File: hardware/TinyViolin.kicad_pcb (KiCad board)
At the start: 2 copper layers, 100 x 80 mm, 44 parts, among them J1 ICSP, J2 503182-1852, SW1 SW_SPDT, SW2 Tactile, SW3 SW_Push, SW4 SW_Push, SW5 SW_Push, SW6 SW_Push, U1 ATmega328-PU, U2 BOOST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

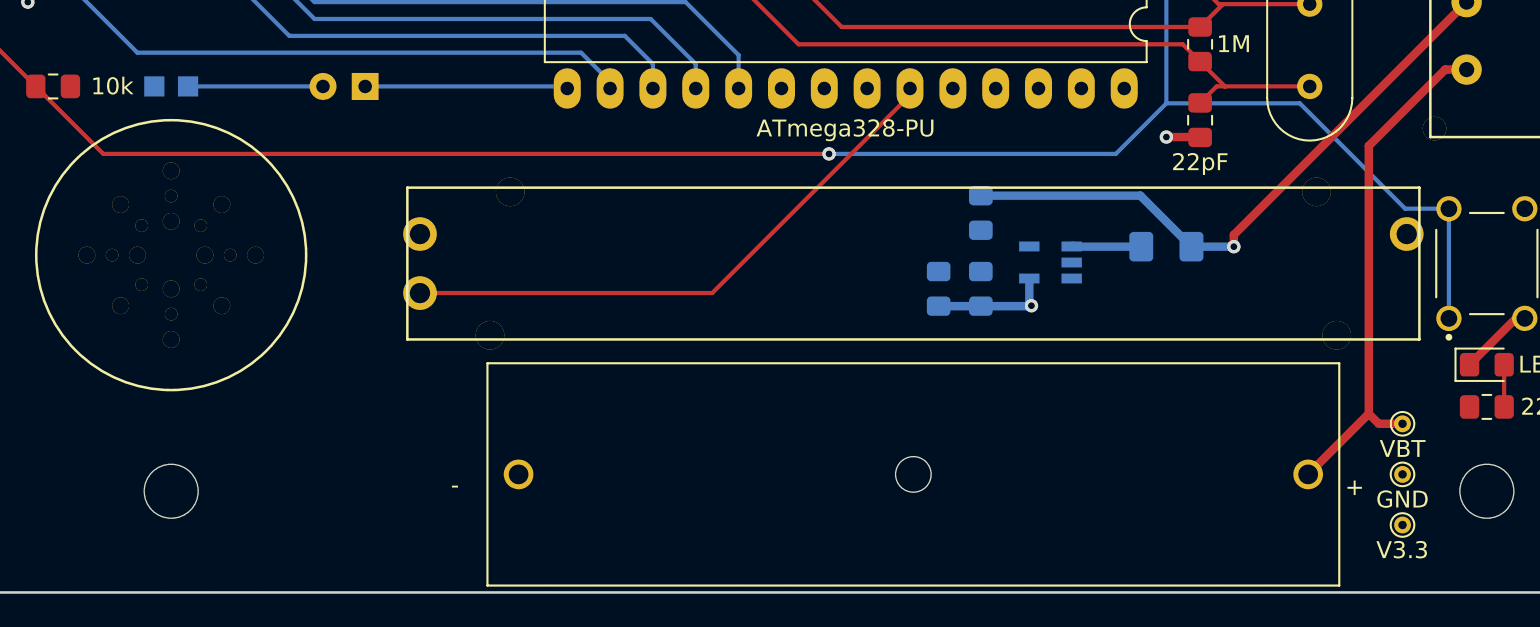
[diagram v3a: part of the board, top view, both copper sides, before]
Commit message: Updated PCB and housing for re-re-manufacture
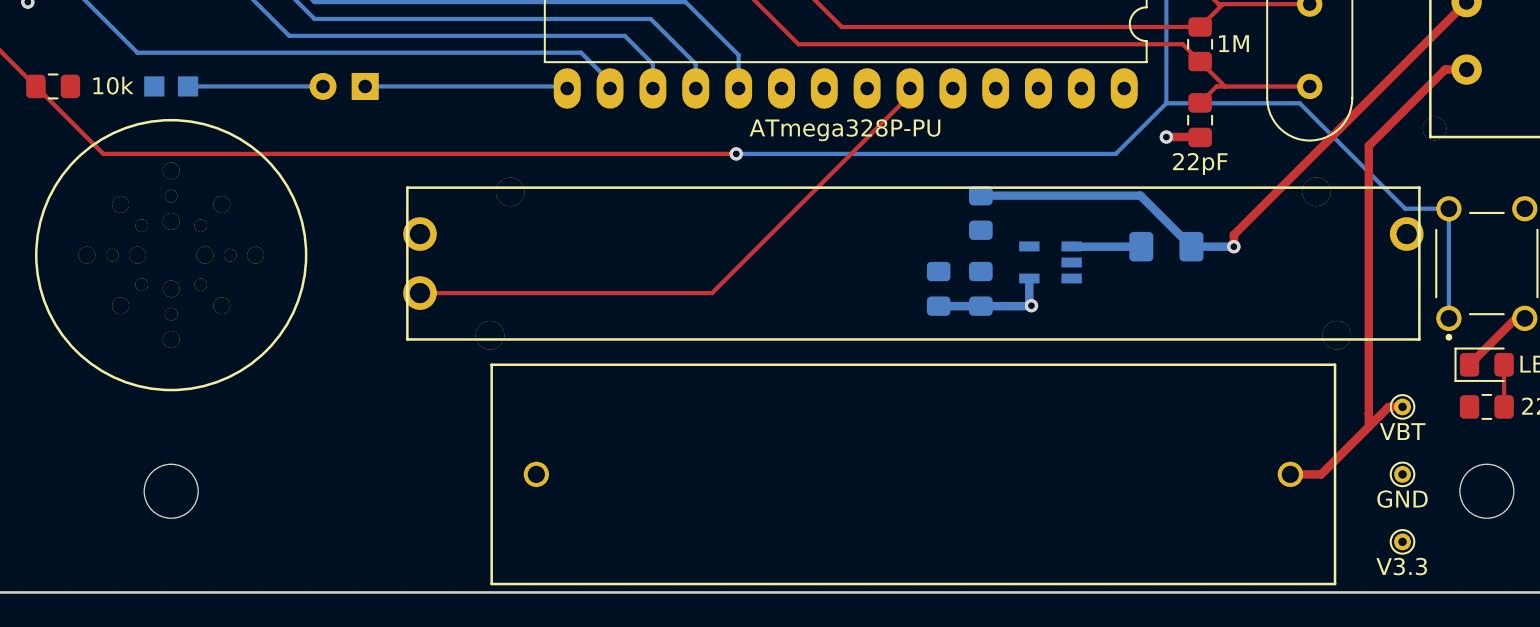
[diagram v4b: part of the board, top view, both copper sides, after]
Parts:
- BT1: value BCAAAPC -> AAA; footprint BAT_BCAAAPC -> 2466:2466
- U1: value ATmega328-PU -> ATmega328P-PU
- moved TP1 1.00 mm to (109.0, 89.0)
- moved TP3 1.00 mm to (109.0, 97.0)
- turned BT1 to 180 degrees
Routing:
- net /BAT: track 30.9 -> 32.0 mm
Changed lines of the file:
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@@
     (thickness 1.6)
     (drawings 5)
-    (tracks 188)
+    (tracks 190)
     (zones 0)
     (modules 44)
@@
     (add_net /VBOOST)
     (add_net GND)
+  )
+  (module 2466:2466 (layer F.Cu)
+    (at 80 93 180)
+    (fp_text reference BT1 (at 0 0.5 180) (layer F.SilkS) hide
+      (effects (font (size 1 1) (thickness 0.15)))
+    )
+    (fp_text value AAA (at 0 -0.5 180) (layer F.Fab)
+      (effects (font (size 1 1) (thickness 0.15)))
+    )
+    (fp_line (start -25 -6.5) (end 25 -6.5) (layer F.SilkS) (width 0.15))
+    (fp_line (start 25 -6.5) (end 25 6.5) (layer F.SilkS) (width 0.15))
+    (fp_line (start 25 6.5) (end -25 6.5) (layer F.SilkS) (width 0.15))
+    (fp_line (start -25 6.5) (end -25 -6.5) (layer F.SilkS) (width 0.15))
+    (pad 1 thru_hole circle (at -22.35 0 180) (size 1.5 1.5) (drill 1.02) (layers *.Cu *.Mask)
+      (net 17 /BAT))
+    (pad 2 thru_hole circle (at 22.35 0 180) (size 1.5 1.5) (drill 1.02) (layers *.Cu *.Mask)
+      (net 9 GND))
   )
   (module Capacitor_THT:CP_Radial_D6.3mm_P2.50mm (layer B.Cu)
@@
     )
   )
-  (module BAT_BCAAAPC (layer F.Cu)
-    (at 80 93)
-    (fp_text reference BT1 (at -22.444 -8.889) (layer F.SilkS) hide
-      (effects (font (size 1.4 1.4) (thickness 0.05)))
-    )
-    (fp_text value BCAAAPC (at -20.555 9.111) (layer F.SilkS) hide
-      (effects (font (size 1.4 1.4) (thickness 0.05)))
-    )
-    (fp_line (start -25.25 -6.59) (end -25.25 6.59) (layer F.SilkS) (width 0.127))
-    (fp_line (start -25.25 6.59) (end 25.25 6.59) (layer F.SilkS) (width 0.127))
-    (fp_line (start 25.25 6.59) (end 25.25 -6.59) (layer F.SilkS) (width 0.127))
-    (fp_line (start 25.25 -6.59) (end -25.25 -6.59) (layer F.SilkS) (width 0.127))
-    (fp_line (start -25.5 -6.84) (end -25.5 6.84) (layer Eco1.User) (width 0.05))
-    (fp_line (start -25.5 6.84) (end 25.5 6.84) (layer Eco1.User) (width 0.05))
-    (fp_line (start 25.5 6.84) (end 25.5 -6.84) (layer Eco1.User) (width 0.05))
-    (fp_line (start 25.5 -6.84) (end -25.5 -6.84) (layer Eco1.User) (width 0.05))
-    (fp_line (start -25.25 -6.59) (end -25.25 6.59) (layer Eco2.User) (width 0.127))
-    (fp_line (start -25.25 6.59) (end 25.25 6.59) (layer Eco2.User) (width 0.127))
-    (fp_line (start 25.25 6.59) (end 25.25 -6.59) (layer Eco2.User) (width 0.127))
-    (fp_line (start 25.25 -6.59) (end -25.25 -6.59) (layer Eco2.User) (width 0.127))
-    (fp_text user + (at 26.162 0.762) (layer F.SilkS)
-      (effects (font (size 1 1) (thickness 0.05)))
-    )
-    (fp_text user + (at 26.162 0.762) (layer Edge.Cuts)
-      (effects (font (size 1 1) (thickness 0.05)))
-    )
-    (fp_text user - (at -27.178 0.635) (layer F.SilkS)
-      (effects (font (size 1 1) (thickness 0.05)))
-    )
-    (fp_text user - (at -27.178 0.635) (layer Edge.Cuts)
-      (effects (font (size 1 1) (thickness 0.05)))
-    )
-    (pad N thru_hole circle (at -23.405 0) (size 1.76 1.76) (drill 1.17) (layers *.Cu *.Mask)
-      (net 9 GND))
-    (pad P thru_hole circle (at 23.405 0) (size 1.76 1.76) (drill 1.17) (layers *.Cu *.Mask)
-      (net 17 /BAT))
-    (pad Hole np_thru_hole circle (at 0 0) (size 2.11 2.11) (drill 2.11) (layers *.Cu *.Mask F.SilkS))
-  )
   (module Capacitor_SMD:C_0805_2012Metric_Pad1.15x1.40mm_HandSolder (layer F.Cu)
     (at 28.5 38.5)
@@
   )
   (module TestPoint:TestPoint_Pad_D1.0mm (layer F.Cu)
-    (at 109 96)
+    (at 109 97)
     (descr "SMD pad as test Point, diameter 1.0mm")
     (tags "test point SMD pad")
@@
   )
   (module TestPoint:TestPoint_Pad_D1.0mm (layer F.Cu)
-    (at 109 90)
+    (at 109 89)
     (descr "SMD pad as test Point, diameter 1.0mm")
     (tags "test point SMD pad")
@@
       (effects (font (size 1 1) (thickness 0.15)))
     )
-    (fp_text value ATmega328-PU (at 10 16.5) (layer F.SilkS)
+    (fp_text value ATmega328P-PU (at 10 16.5) (layer F.SilkS)
       (effects (font (size 1 1) (thickness 0.15)))
     )
@@
   (gr_line (start 120 100) (end 20 100) (layer Edge.Cuts) (width 0.15))
   (gr_line (start 120 20) (end 120 100) (layer Edge.Cuts) (width 0.15))
-  (via (at 99 79.5) (size 0.8) (drill 0.4) (layers F.Cu B.Cu) (net 18))
   (segment (start 64.56 69.72) (end 64.56 70.12) (width 0.25) (layer B.Cu) (net 1))
   (segment (start 62.89 67) (end 43 67) (width 0.25) (layer B.Cu) (net 1))
@@
   (segment (start 115.725 83.75) (end 116.25 83.75) (width 0.5) (layer F.Cu) (net 9))
   (segment (start 112.975 86.5) (end 115.725 83.75) (width 0.5) (layer F.Cu) (net 9))
-  (via (at 75 74) (size 0.8) (drill 0.4) (layers F.Cu B.Cu) (net 10))
+  (via (at 69.5 74) (size 0.8) (drill 0.4) (layers F.Cu B.Cu) (net 10))
   (segment (start 93.55 62.5) (end 92.5 62.5) (width 0.25) (layer B.Cu) (net 10))
   (segment (start 95 63.95) (end 93.55 62.5) (width 0.25) (layer B.Cu) (net 10))
@@
   (segment (start 109.158998 77.25) (end 102.908998 71) (width 0.25) (layer B.Cu) (net 10))
   (segment (start 111.75 77.25) (end 109.158998 77.25) (width 0.25) (layer B.Cu) (net 10))
-  (segment (start 92 74) (end 75 74) (width 0.25) (layer B.Cu) (net 10))
-  (segment (start 95 71) (end 92 74) (width 0.25) (layer B.Cu) (net 10))
   (segment (start 25 55.282081) (end 25 54.08) (width 0.25) (layer F.Cu) (net 10))
   (segment (start 25 67.025) (end 25 55.282081) (width 0.25) (layer F.Cu) (net 10))
   (segment (start 31.975 74) (end 25 67.025) (width 0.25) (layer F.Cu) (net 10))
-  (segment (start 75 74) (end 31.975 74) (width 0.25) (layer F.Cu) (net 10))
+  (segment (start 69.5 74) (end 31.975 74) (width 0.25) (layer F.Cu) (net 10))
+  (segment (start 92 74) (end 95 71) (width 0.25) (layer B.Cu) (net 10))
+  (segment (start 69.5 74) (end 92 74) (width 0.25) (layer B.Cu) (net 10))
   (segment (start 98.475 70) (end 103.5 70) (width 0.25) (layer F.Cu) (net 11))
   (segment (start 97 68.525) (end 98.475 70) (width 0.25) (layer F.Cu) (net 11))
@@
   (segment (start 111.527208 69) (end 107 73.527208) (width 0.5) (layer F.Cu) (net 17))
   (segment (start 112.8 69) (end 111.527208 69) (width 0.5) (layer F.Cu) (net 17))
-  (segment (start 107 89.405) (end 103.405 93) (width 0.5) (layer F.Cu) (net 17))
   (segment (start 107 73.527208) (end 107 89.405) (width 0.5) (layer F.Cu) (net 17))
-  (segment (start 107.595 90) (end 107 89.405) (width 0.5) (layer F.Cu) (net 17))
-  (segment (start 109 90) (end 107.595 90) (width 0.5) (layer F.Cu) (net 17))
+  (segment (start 107 90.179507) (end 107 89.405) (width 0.5) (layer F.Cu) (net 17))
+  (segment (start 104.179507 93) (end 107 90.179507) (width 0.5) (layer F.Cu) (net 17))
+  (segment (start 102.935 93) (end 104.179507 93) (width 0.5) (layer F.Cu) (net 17))
+  (segment (start 108.179507 89) (end 107 90.179507) (width 0.5) (layer F.Cu) (net 17))
+  (segment (start 109 89) (end 108.179507 89) (width 0.5) (layer F.Cu) (net 17))
+  (via (at 99 79.5) (size 0.8) (drill 0.4) (layers F.Cu B.Cu) (net 18))
   (segment (start 98.96347 79.43653) (end 99 79.4) (width 0.5) (layer B.Cu) (net 18))
   (segment (start 112.8 65) (end 99 78.8) (width 0.5) (layer F.Cu) (net 18))
